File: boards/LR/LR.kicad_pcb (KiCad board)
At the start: 2 copper layers, 46 parts, among them X1 B5B-XH-A, X2 B5B-XH-A, X3 B5B-XH-A, X4 B5B-XH-A, X5 клеммы, X6 клеммы, X7 клеммы, X8 клеммы, X9 B4B-XH-A

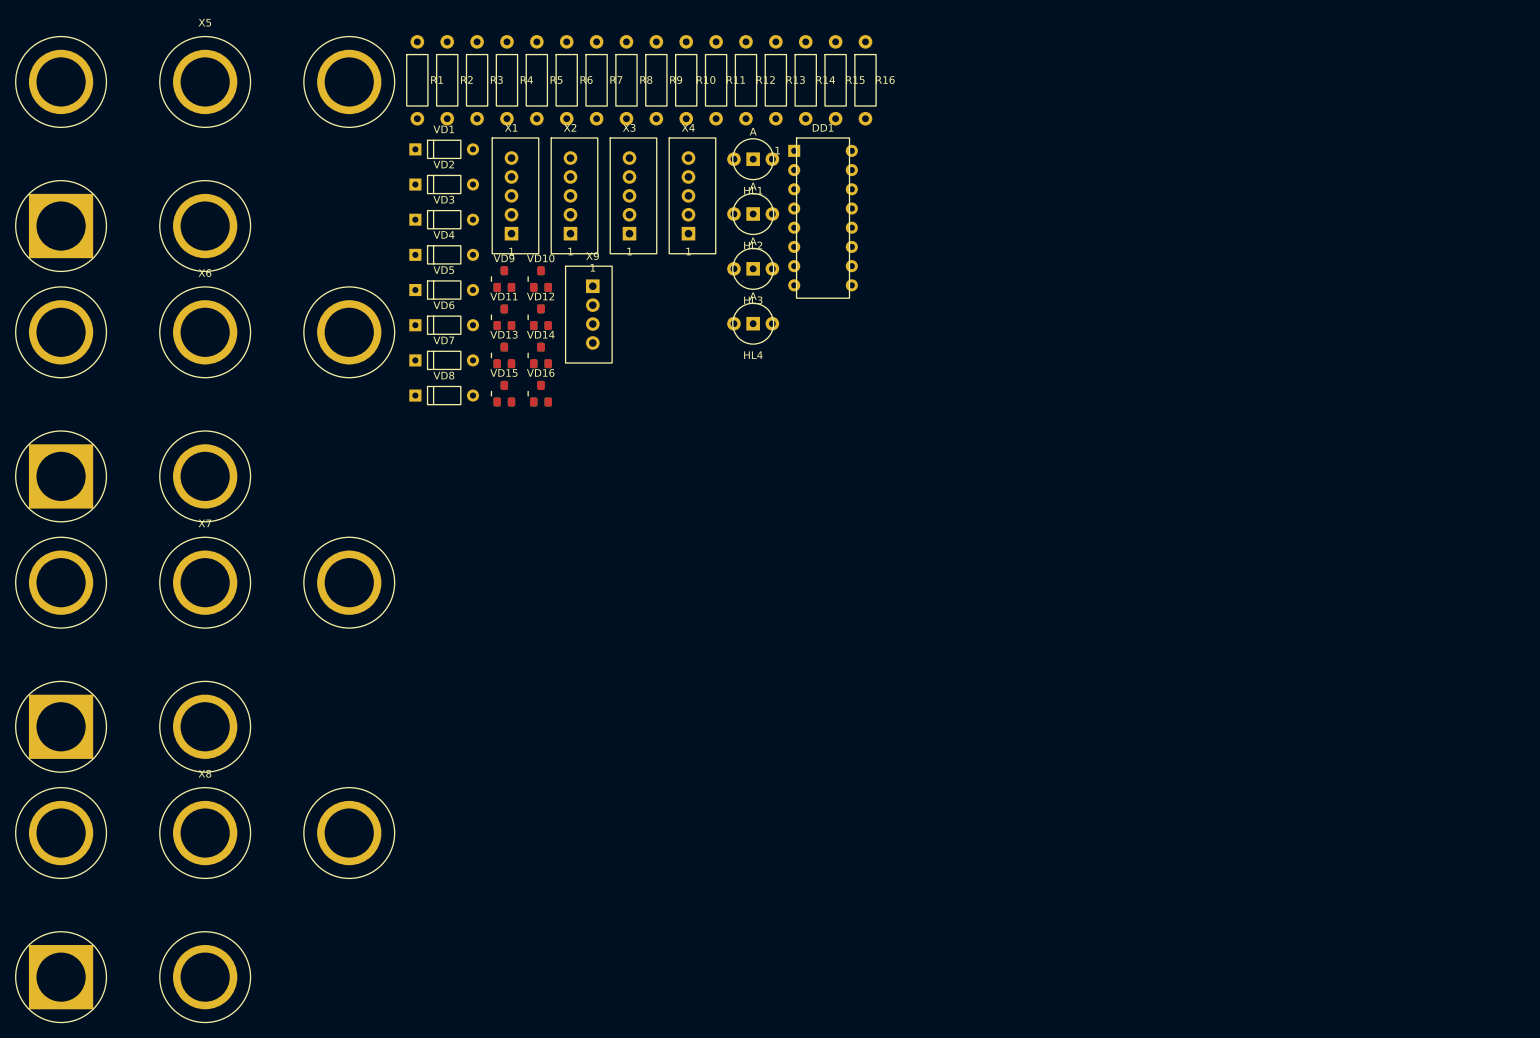
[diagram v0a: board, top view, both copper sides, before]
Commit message: Платы PS, MC, CH, LR: расстановка, трассировка, 3D-модели посадочных мест
PS:
- разведена по расстановке из файла: +24V_IN 6 мм (участок у K1 — 4 мм),
  шина +24V 6 мм с отводами 3 мм, +5P 2 мм, остров U2 1,5 мм;
  заливка GND_P на B.Cu, вырез заливки под островом, вырезы ⌀8 у крепежа
- классы цепей в PS.kicad_pro: Default, Power5, Power24, Island
- U1: посадочное место под модуль XL4015E 54 × 24 × 15 на штырях
  (пятаки IN/OUT, 2 стойки М3) по чертежу продавца; переразведены
  OUT+ и отвод +24V к IN+

MC:
- X5 перенесён, переразведены KH, +5P, GND_P в этой зоне
- FU1: место под Bourns MF-R110 (корпус 8,9 × 3,0 × 14,0)

CH:
- K1…K5, X5: места исправлены по datasheet (NRP-02, HF49FD, JST VH),
  переразведены цепи реле

LR:
- плата перекомпонована: X5…X8 — B5B-XH-A, как X1…X4; группы M1…M4
  по одному образцу (индикатор, разъём, защита в два ряда);
  X1…X4, X9 и DD1 на нижней стороне
- контур 176 × 59, 6 отверстий М3; разведена: сигналы F.Cu,
  GND_L заливкой B.Cu
- scripts/gen_LR_pcb.py удалён: описывал прежнюю раскладку с клеммами

Схемы:
- CH: X5 — JST VH (таблица Tbl_X5_CH_VH); MC: X3 — B4B-XH-A
  (кнопка KH с индикатором); PS: X11 убран; LR: у X5…X8 место
  B5B-XH-A
- sch_common: генератор не перезаписывает файл, сохранённый KiCad,
  без --force

3D-модели (lib/3dmodels):
- упрощённые по чертежам datasheet: NRP-02, HF49FD, NRP-15 (корпус),
  JST B2P-VH, Mornsun/K-CUT URB2405YMD (U2), Talema DPO-3.0-22 (кольцо
  лежит), Bourns MF-R110
- из библиотеки KiCad: PinSocket 1×3, 1×4, 1×12, Phoenix MKDS-1,5-2
- docs/3D-модели.md — источники размеров и что сверить

База компонентов: E-083 — Bourns MF-R110 (Ihold 1,1 А), «Выбран»;
csv перевыгружены
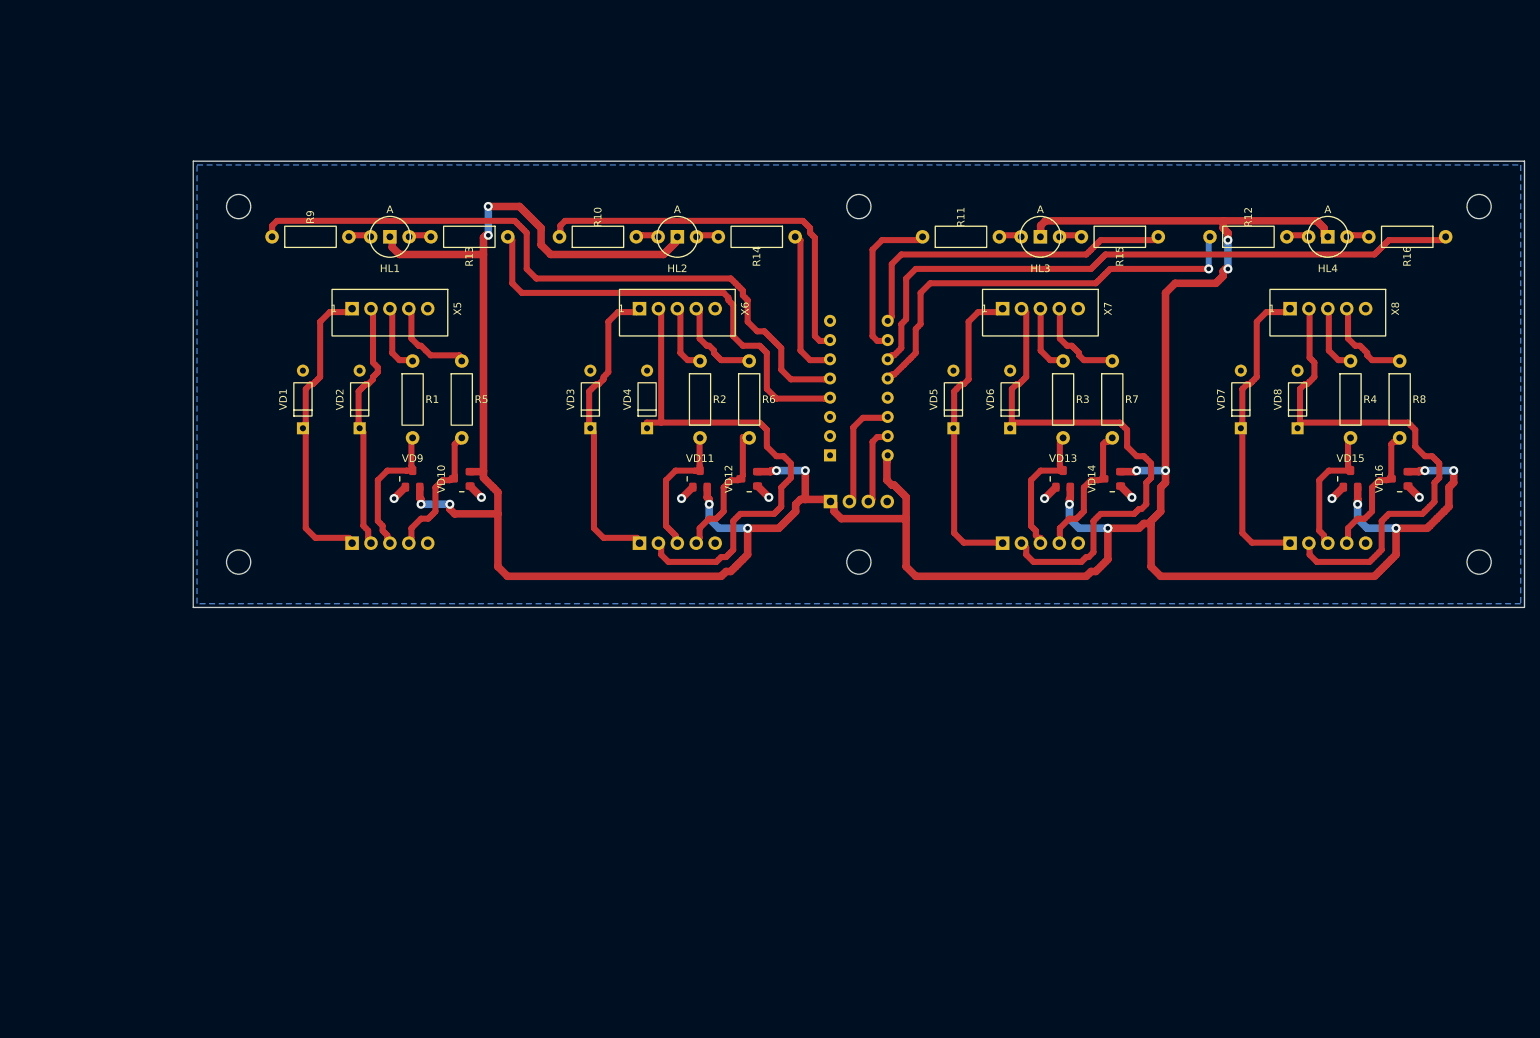
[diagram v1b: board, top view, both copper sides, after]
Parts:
- added H1: M3, manipulator:MountingHole_3.2mm_M3, F.Cu at (66.0, 51.5)
- added H2: M3, manipulator:MountingHole_3.2mm_M3, F.Cu at (148.0, 51.5)
- added H3: M3, manipulator:MountingHole_3.2mm_M3, F.Cu at (230.0, 51.5)
- added H4: M3, manipulator:MountingHole_3.2mm_M3, F.Cu at (66.0, 98.5)
- added H5: M3, manipulator:MountingHole_3.2mm_M3, F.Cu at (148.0, 98.5)
- added H6: M3, manipulator:MountingHole_3.2mm_M3, F.Cu at (230.0, 98.5)
- DD1, X1, X2, X3, X4, X9: moved to B.Cu
- X5, X6, X7, X8: footprint manipulator:TermGroup_5x_Banana4 -> manipulator:JST_XH_B5B-XH-A_L
- moved X8 168.1 mm to (210.0, 65.0), turned to -90 degrees
- moved X7 119.5 mm to (172.0, 65.0), turned to -90 degrees
- moved R4 119.2 mm to (213.0, 77.0)
- moved VD16 114.1 mm to (219.5, 87.5), turned to 90 degrees
- moved VD8 112.8 mm to (206.0, 77.0), turned to 90 degrees
- moved VD15 112.4 mm to (213.0, 87.5)
- moved R8 110.6 mm to (219.5, 77.0)
- moved VD7 105.5 mm to (198.5, 77.0), turned to 90 degrees
- moved X4 96.2 mm to (210.0, 96.0), turned to 90 degrees
- moved R3 88.2 mm to (175.0, 77.0)
- moved R7 80.2 mm to (181.5, 77.0)
- moved VD14 77.3 mm to (181.5, 87.5), turned to 90 degrees
- moved HL4 76.8 mm to (210.0, 55.5)
- moved VD13 75.7 mm to (175.0, 87.5)
- moved VD6 75.5 mm to (168.0, 77.0), turned to 90 degrees
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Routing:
- net 3V3: track 0.00 -> 422.3 mm, vias 0 -> 18
- net Net-(DD1-P1): track 0.00 -> 90.7 mm
- net Net-(DD1-P6): track 0.00 -> 85.6 mm
- net Net-(VD8-K): track 0.00 -> 69.2 mm
- net Net-(VD6-K): track 0.00 -> 69.2 mm
- net Net-(VD4-K): track 0.00 -> 67.9 mm
- net Net-(DD1-P0): track 0.00 -> 60.2 mm
- net Net-(DD1-P7): track 0.00 -> 57.0 mm, vias 0 -> 1
- net Net-(DD1-P3): track 0.00 -> 52.0 mm
- net Net-(DD1-P4): track 0.00 -> 44.5 mm
- net Net-(VD5-K): track 0.00 -> 41.0 mm
- net Net-(VD7-K): track 0.00 -> 40.9 mm
- net Net-(VD3-K): track 0.00 -> 40.6 mm
- net Net-(VD1-K): track 0.00 -> 40.5 mm
- net Net-(VD2-K): track 0.00 -> 33.1 mm
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- added copper zone on B.Cu, net GND_L
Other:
- board outline added: 176 x 59 mm

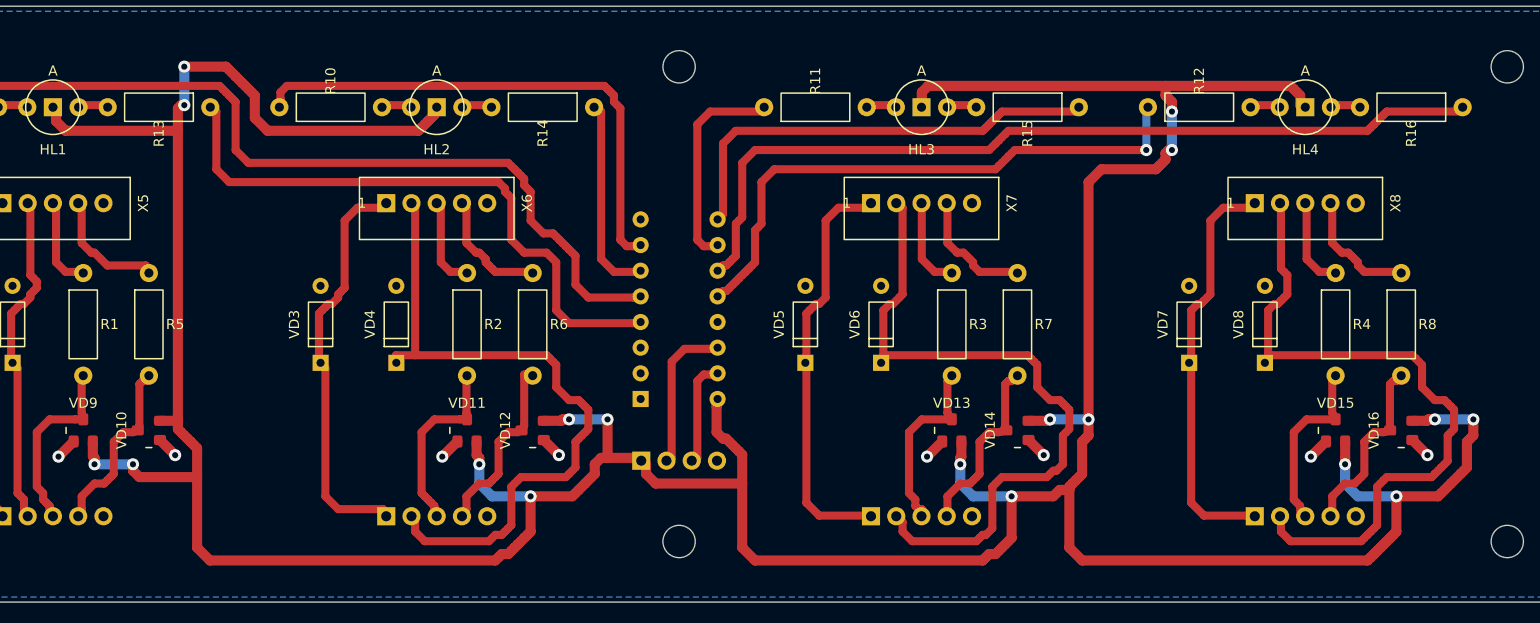
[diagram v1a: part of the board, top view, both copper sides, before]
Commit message: Документы плат PS, MC, CH, LR; обозначения по схеме кафедры, наименования плат
- Документы плат PS, MC, CH, LR: перечень элементов, схема Э3, чертёж
  печатной платы, сборочный чертёж, спецификация (docs/<КОД>/)
- .gitignore: выпущенные документы docs/<КОД>/*.pdf хранятся в истории
- 3D-модели плат boards/<КОД>/<КОД>.step — исходные данные для проекций СБ
- Обозначения СМ7.02.ПП.ДД.00: ПЭ3, Э3, СБ — .00.00, плата печатная — .01.00,
  спецификация платы — .00.00 без аббревиатуры; правила в CLAUDE.md
- scripts/doc_titles.py: обозначения, наименования, подписи и основная надпись
  в одном месте; генераторы схем и плат берут их оттуда
- scripts/gen_pe3.py: перечень элементов ПЭ3 (А4, ГОСТ 2.701, 2.104)
- Наименования: «Манипулятор для лабораторных работ», платы питания,
  микроконтроллера, силовой части, режима ЛР (README, board-partition, генераторы)
- Схемы PS, MC, CH, LR перегенерированы: основная надпись из doc_titles,
  BaseID разъёмов E-092, E-096, E-097, E-098
- LR: X5…X8 — разъёмы к панели ЛР (E-098) вместо клемм E-051
- База компонентов: тип и допуск резисторов в наименовании, новые позиции
  E-096…E-098, E-051 исключена
- Платы: настройки вывода на печать; LR — дорожки и заливка зон
- Пояснительная записка курсового проекта обновлена
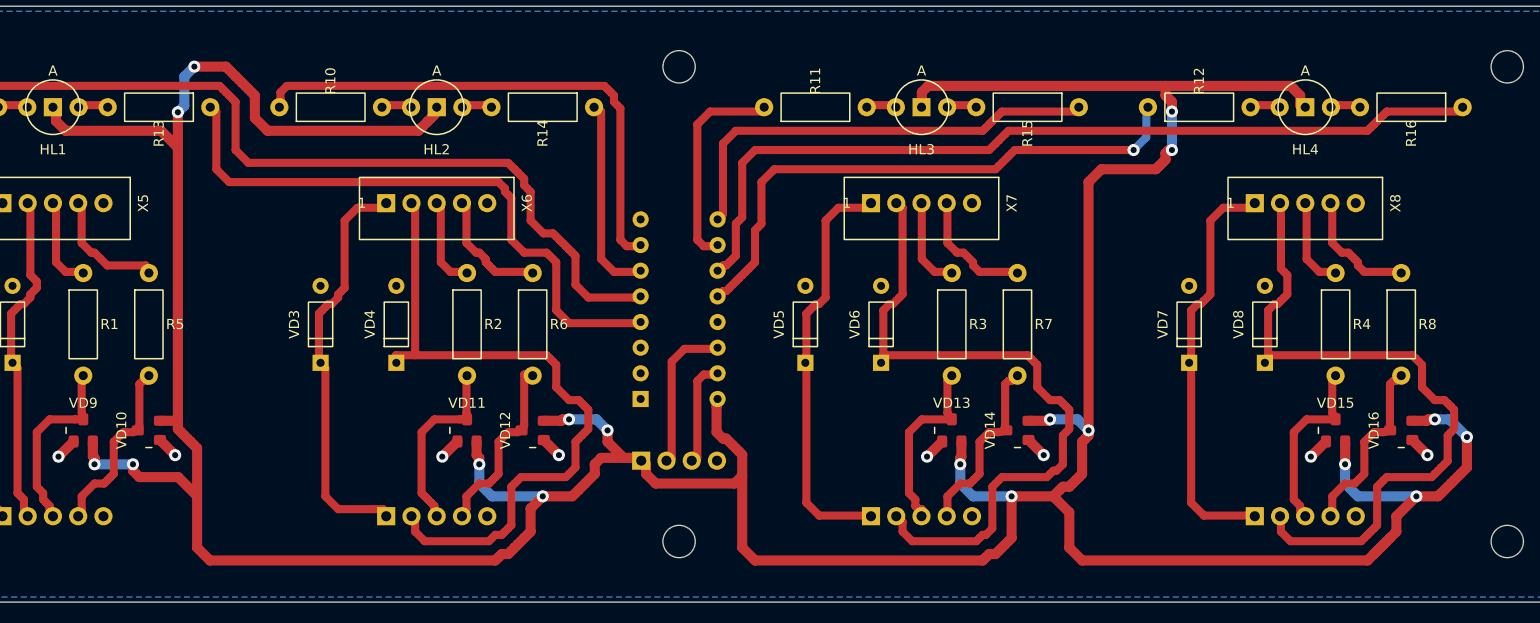
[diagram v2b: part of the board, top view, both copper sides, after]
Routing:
- net Net-(DD1-P7): track 57.0 -> 56.3 mm
- net 3V3: track 422.3 -> 423.0 mm
